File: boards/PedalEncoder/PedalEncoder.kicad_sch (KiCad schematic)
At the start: 10 parts

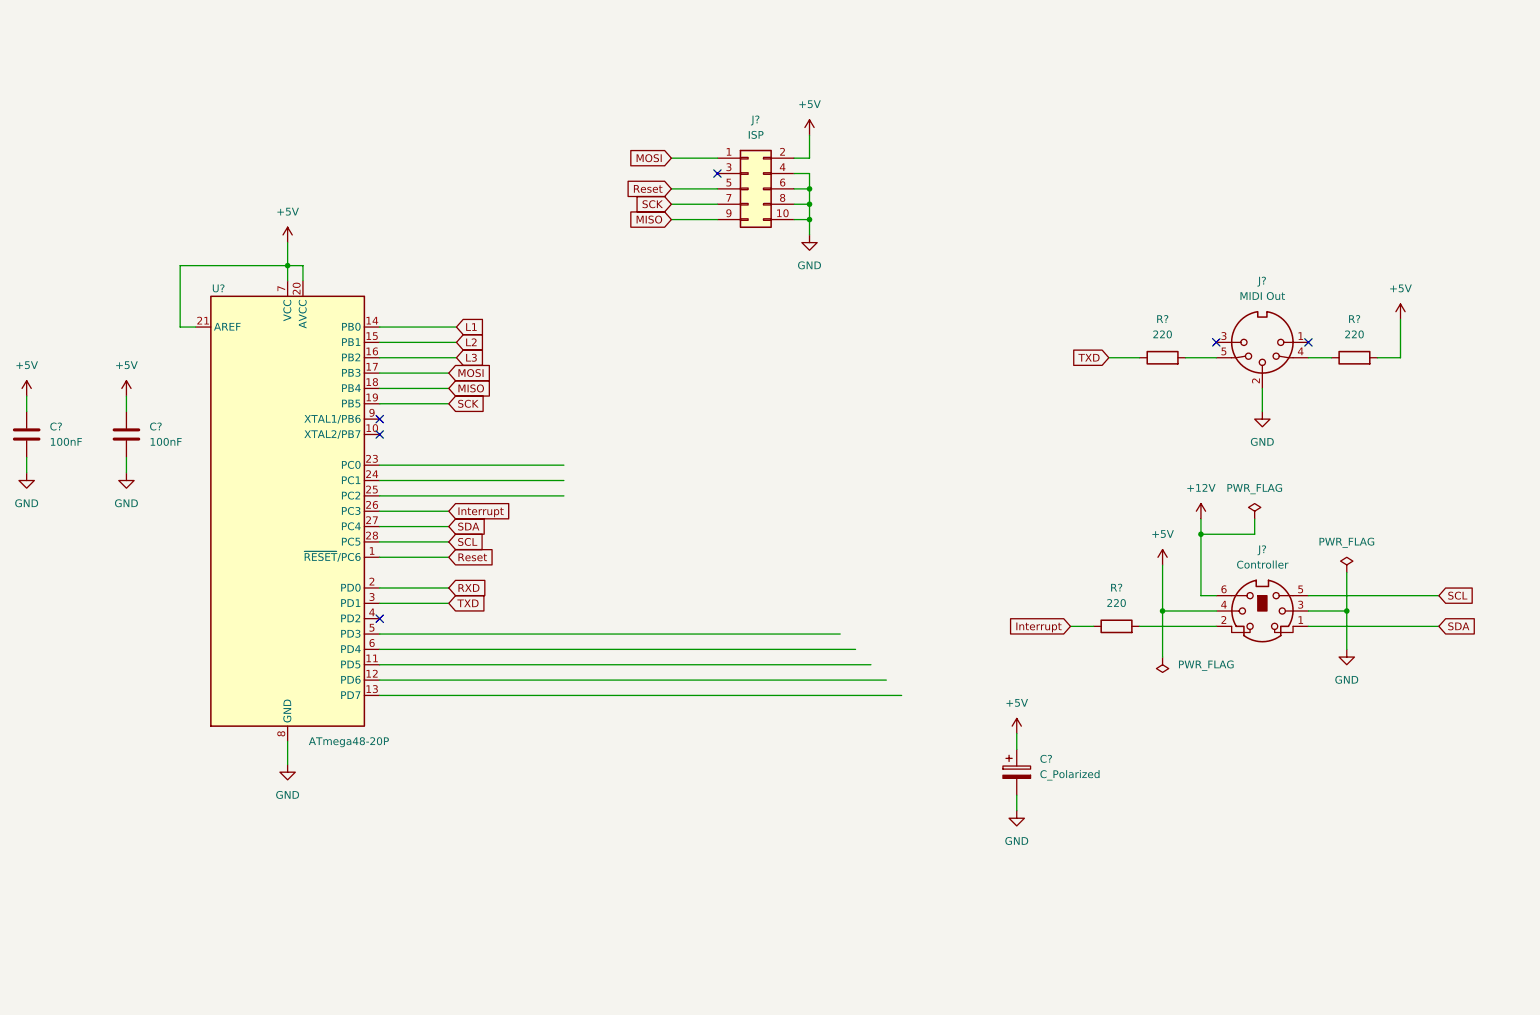
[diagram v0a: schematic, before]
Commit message: Added schematics of pedal board controller
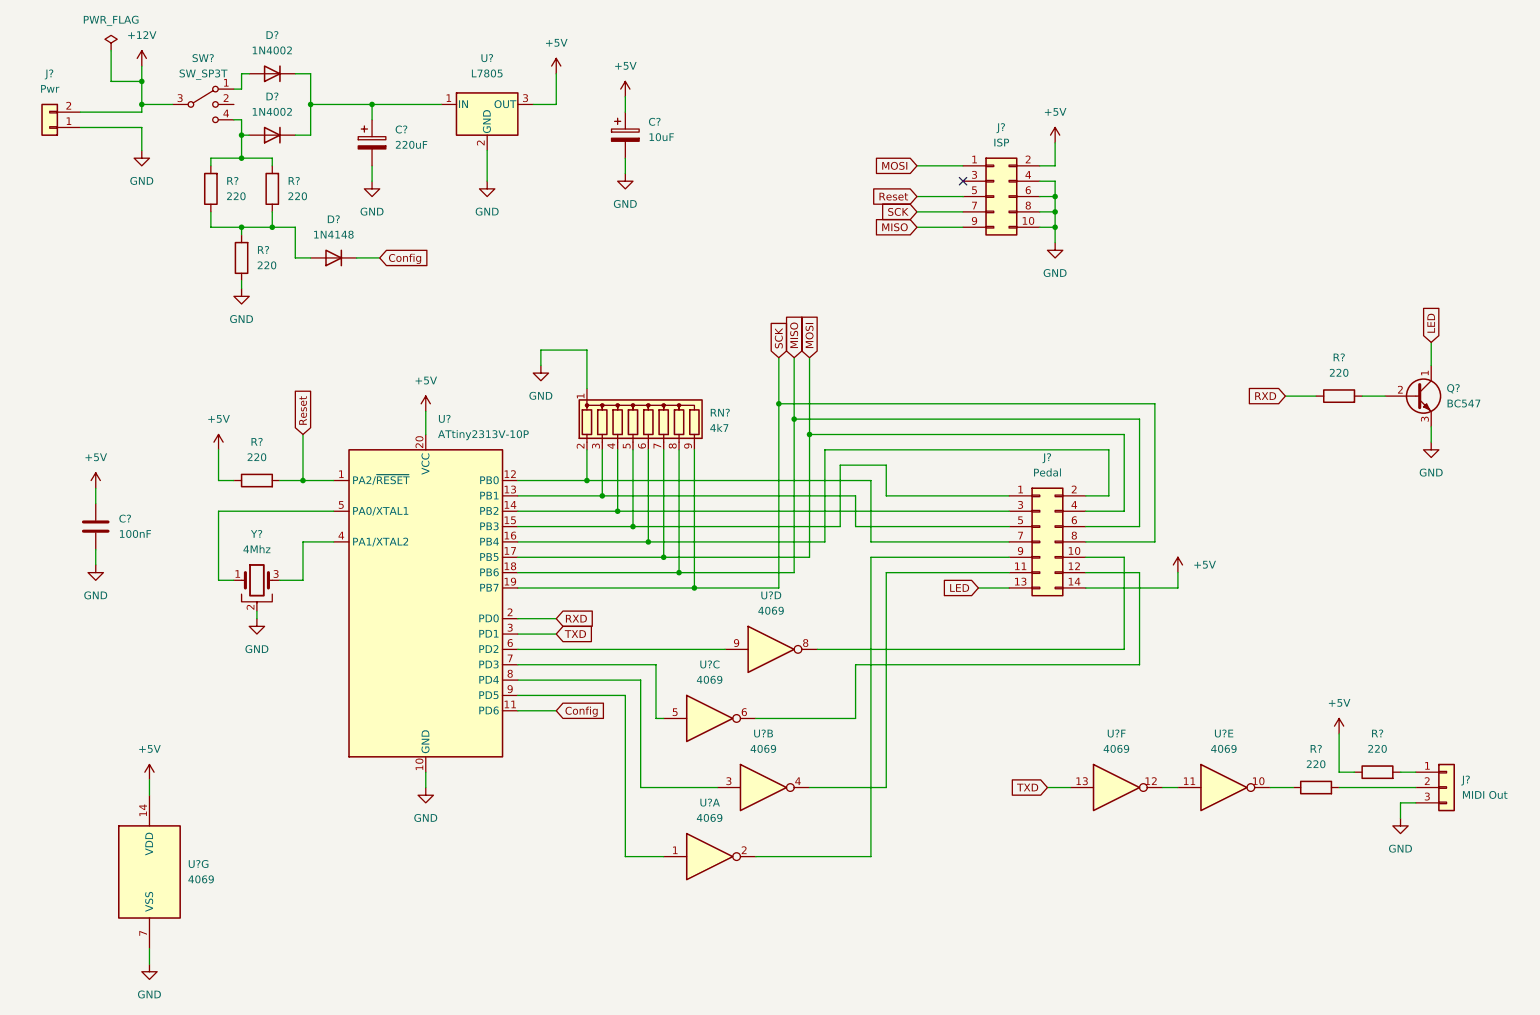
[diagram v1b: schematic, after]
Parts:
- removed C?: 100nF, symbol Device:C
- removed J?: Controller, symbol Connector:Mini-DIN-6
- removed J?: MIDI Out, symbol Connector:DIN-5_180degree
- removed R?: 220, Resistor_THT:R_Axial_DIN0204_L3.6mm_D1.6mm_P2.54mm_Vertical, symbol Device:R
- removed U?: ATmega48-20P, Package_DIP:DIP-28_W7.62mm, symbol MCU_Microchip_ATmega:ATmega48-20P
- added C?: 220uF, symbol Device:C_Polarized
- added D? (x2): 1N4002, Diode_THT:D_DO-41_SOD81_P10.16mm_Horizontal, symbol Diode:1N4002
- added D?: 1N4148, Diode_THT:D_DO-35_SOD27_P7.62mm_Horizontal, symbol Diode:1N4148
- added J?: MIDI Out, symbol Connector_Generic:Conn_01x03
- added J?: Pwr, symbol Connector_Generic:Conn_01x02
- added J?: Pedal, symbol Connector_Generic:Conn_02x07_Odd_Even
- added Q?: BC547, Package_TO_SOT_THT:TO-92_Inline, symbol Transistor_BJT:BC547
- added R? (x5): 220, Resistor_THT:R_Axial_DIN0204_L3.6mm_D1.6mm_P2.54mm_Vertical, symbol Device:R
- added RN?: 4k7, Resistor_THT:R_Array_SIP9, symbol Device:R_Network08
- added SW?: SW_SP3T, symbol Switch:SW_SP3T
- added U?: L7805, symbol Regulator_Linear:L7805
- added U? (x7): 4069, symbol 4xxx:4069
- added U?: ATtiny2313V-10P, Package_DIP:DIP-20_W7.62mm, symbol MCU_Microchip_ATtiny:ATtiny2313V-10P
- added Y?: 4Mhz, symbol Device:Crystal_GND2
- C?: value C_Polarized -> 10uF
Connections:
- net +12V: now also J?.2 (Pin_2), SW?.3
- net +5V: now also R?.1, J?.14 (Pin_14), R?.1, U?.14 (VDD), U?.20 (VCC), U?.3 (OUT); no longer R?.2
- net GND: now also C?.2, J?.1 (Pin_1), J?.3 (Pin_3), Q?.3 (E), R?.1, RN?.1 (common), U?.10 (GND), U?.2 (GND), U?.7 (VSS), Y?.2
- net MISO: now also J?.6 (Pin_6), RN?.8 (R7), U?.18 (PB6)
- net MOSI: now also J?.4 (Pin_4), RN?.7 (R6), U?.17 (PB5)
- net RXD: now also R?.1, U?.2 (PD0)
- net Reset: now also R?.2, U?.1 (PA2/~{RESET})
- net SCK: now also J?.8 (Pin_8), RN?.9 (R8), U?.19 (PB7)
- net TXD: now also U?.13, U?.3 (PD1); no longer R?.1
- net at R?.1: now also U?.10
- net at R?.2: now also J?.1 (Pin_1)
- new net: J?.7 (Pin_7), RN?.2 (R1), U?.12 (PB0)
- new net: J?.5 (Pin_5), RN?.3 (R2), U?.13 (PB1)
- new net: J?.3 (Pin_3), RN?.4 (R3), U?.14 (PB2)
- new net: J?.1 (Pin_1), RN?.5 (R4), U?.15 (PB3)
- new net: J?.2 (Pin_2), RN?.6 (R5), U?.16 (PB4)
- new net: C?.1, D?.1 (K), D?.1 (K), U?.1 (IN)
- new net: D?.2 (A), R?.2, R?.2, SW?.4
- new net: J?.2 (Pin_2), R?.2
- new net: D?.2 (A), SW?.1
- new net: Q?.2 (B), R?.2
- new net: D?.2 (A), R?.1, R?.1, R?.2
- new net: J?.10 (Pin_10), U?.8
- new net: U?.6 (PD2), U?.9
- new net: U?.5 (PA0/XTAL1), Y?.1
- new net: U?.4 (PA1/XTAL2), Y?.3
- new net: U?.5, U?.7 (PD3)
- new net: J?.12 (Pin_12), U?.6
- new net: U?.11, U?.12
- new net: U?.3, U?.8 (PD4)
- new net: U?.1, U?.9 (PD5)
- new net: J?.9 (Pin_9), U?.2
- new net: J?.11 (Pin_11), U?.4
- new net Config: D?.1 (K), U?.11 (PD6)
- new net LED: J?.13 (Pin_13), Q?.1 (C)
- no-connect marks 6 -> 1
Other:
- moved on the sheet: C?, J?, R?

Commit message: Updated Pedal Encoder to use UART from ToeStudEncoder
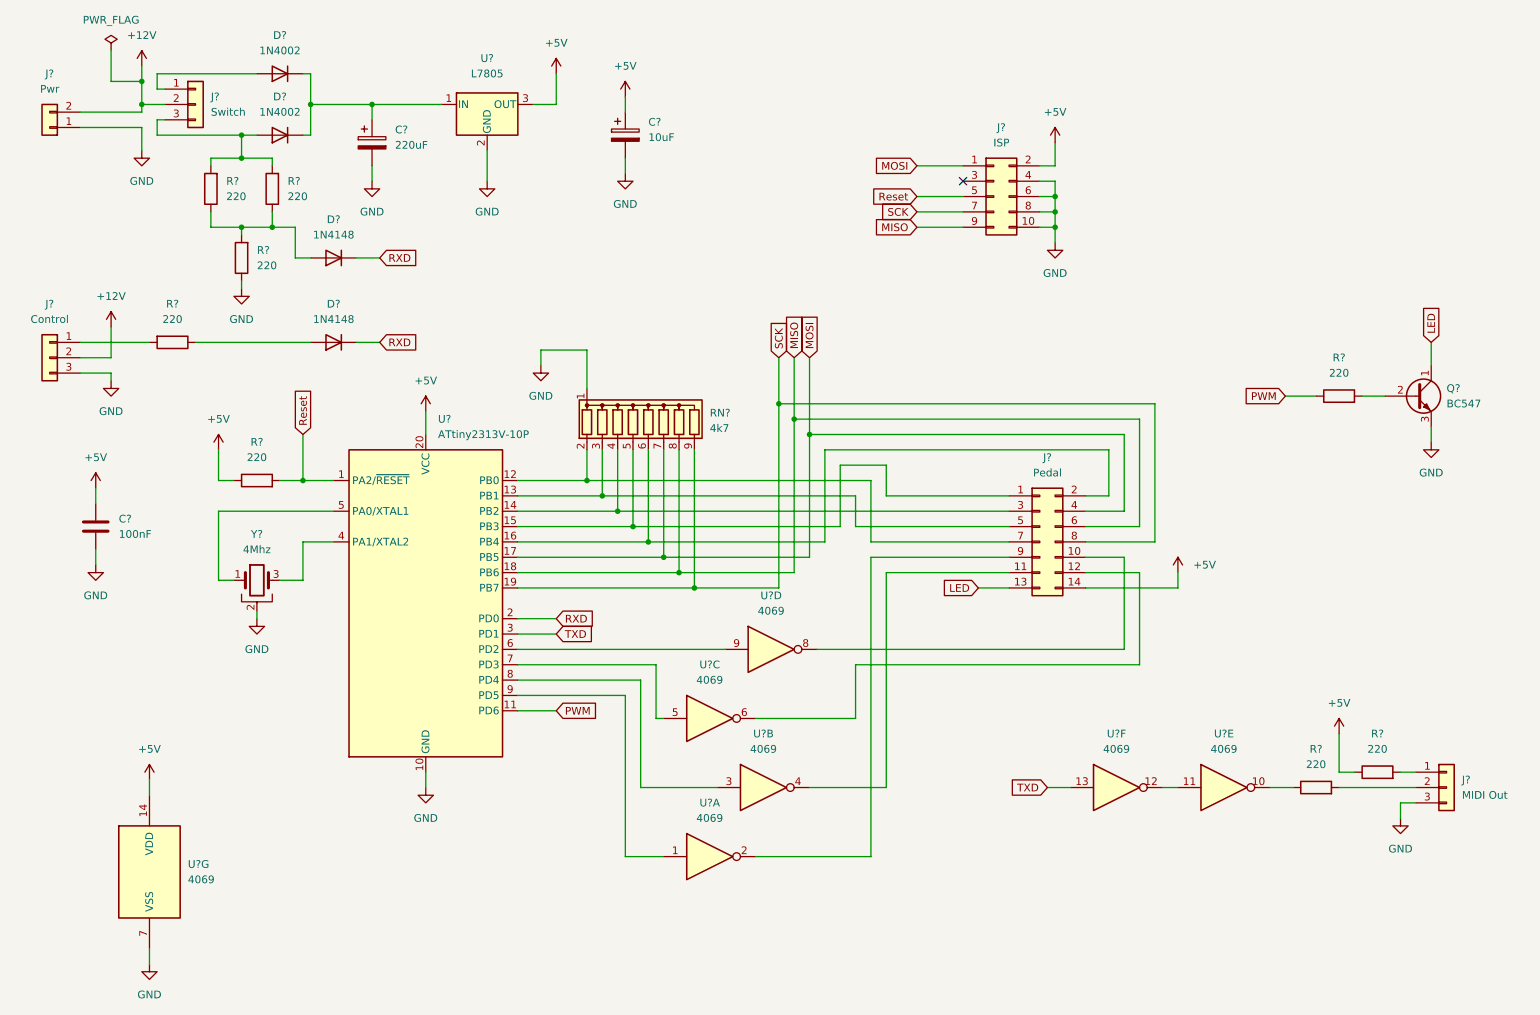
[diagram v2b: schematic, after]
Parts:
- removed SW?: SW_SP3T, symbol Switch:SW_SP3T
- added D?: 1N4148, Diode_THT:D_DO-35_SOD27_P7.62mm_Horizontal, symbol Diode:1N4148
- added J?: Control, symbol Connector_Generic:Conn_01x03
- added J?: Switch, symbol Connector_Generic:Conn_01x03
- added R?: 220, Resistor_THT:R_Axial_DIN0204_L3.6mm_D1.6mm_P2.54mm_Vertical, symbol Device:R
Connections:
- net +12V: now also J?.2 (Pin_2), J?.2 (Pin_2)
- net GND: now also J?.3 (Pin_3)
- net RXD: now also D?.1 (K), D?.1 (K); no longer R?.1
- net at D?.2 (A), R?.2, R?.2: now also J?.3 (Pin_3)
- net at D?.2 (A): now also J?.1 (Pin_1)
- net Config renamed PWM
- net PWM: now also R?.1; no longer D?.1 (K)
- new net: D?.2 (A), R?.1
- new net: J?.1 (Pin_1), R?.2
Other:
- moved on the sheet: D?

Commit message: Renamed PCBs and updated to KiCAD 7.0
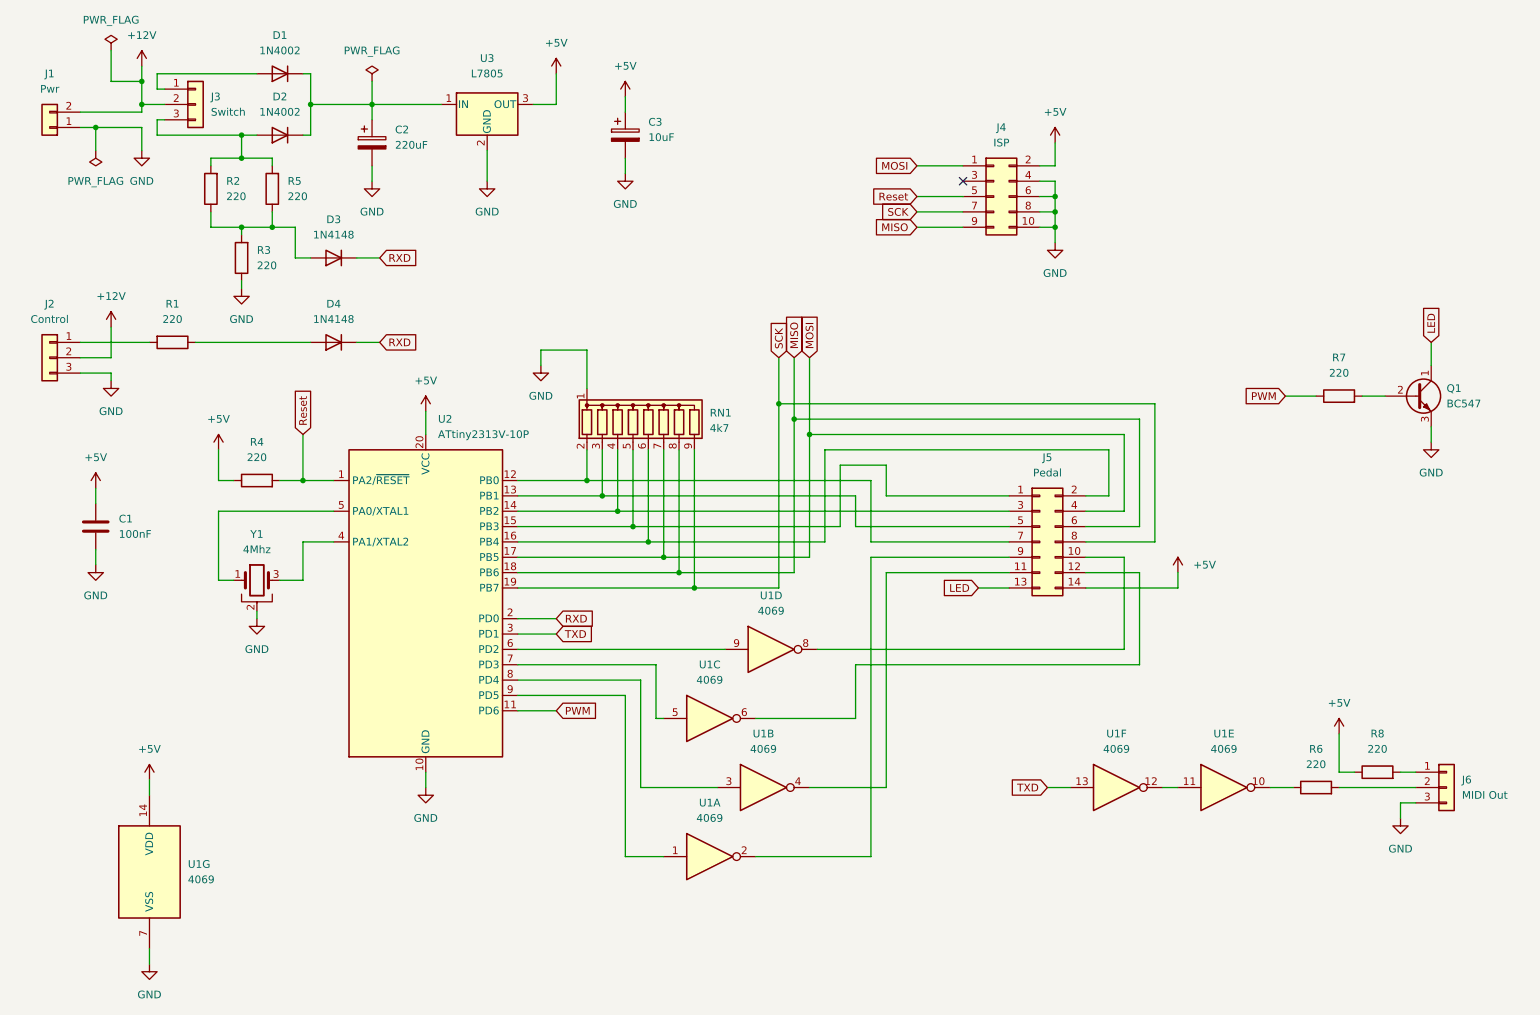
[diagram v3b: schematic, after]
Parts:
- C1: renamed from C?; footprint (none) -> Capacitor_THT:C_Disc_D7.5mm_W2.5mm_P5.00mm
- C2: renamed from C?; footprint (none) -> Capacitor_THT:CP_Radial_D10.0mm_P5.00mm
- C3: renamed from C?; footprint (none) -> Capacitor_THT:CP_Radial_D8.0mm_P2.50mm
- J1: renamed from J?; footprint (none) -> Connector_PinSocket_2.54mm:PinSocket_1x02_P2.54mm_Vertical
- J2, J3, J6: renamed from J?; footprint (none) -> Connector_PinHeader_2.54mm:PinHeader_1x03_P2.54mm_Vertical
- J5: renamed from J?; footprint (none) -> Connector_PinHeader_2.54mm:PinHeader_2x07_P2.54mm_Vertical
- U1: renamed from U?; footprint (none) -> Package_DIP:DIP-14_W7.62mm
- U3: renamed from U?; footprint (none) -> Package_TO_SOT_THT:TO-220-3_Vertical
- Y1: renamed from Y?; footprint (none) -> Crystal:Crystal_HC49-U-3Pin_Vertical
- gave numbers to parts that had none: 16
